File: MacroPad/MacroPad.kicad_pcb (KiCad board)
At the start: 2 copper layers, 120 x 100 mm, 27 parts, among them SW1 CherryMX, SW10 CherryMX, SW11 CherryMX, SW12 CherryMX, SW2 CherryMX, SW3 CherryMX, SW4 CherryMX, SW5 CherryMX, SW6 CherryMX, SW7 CherryMX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

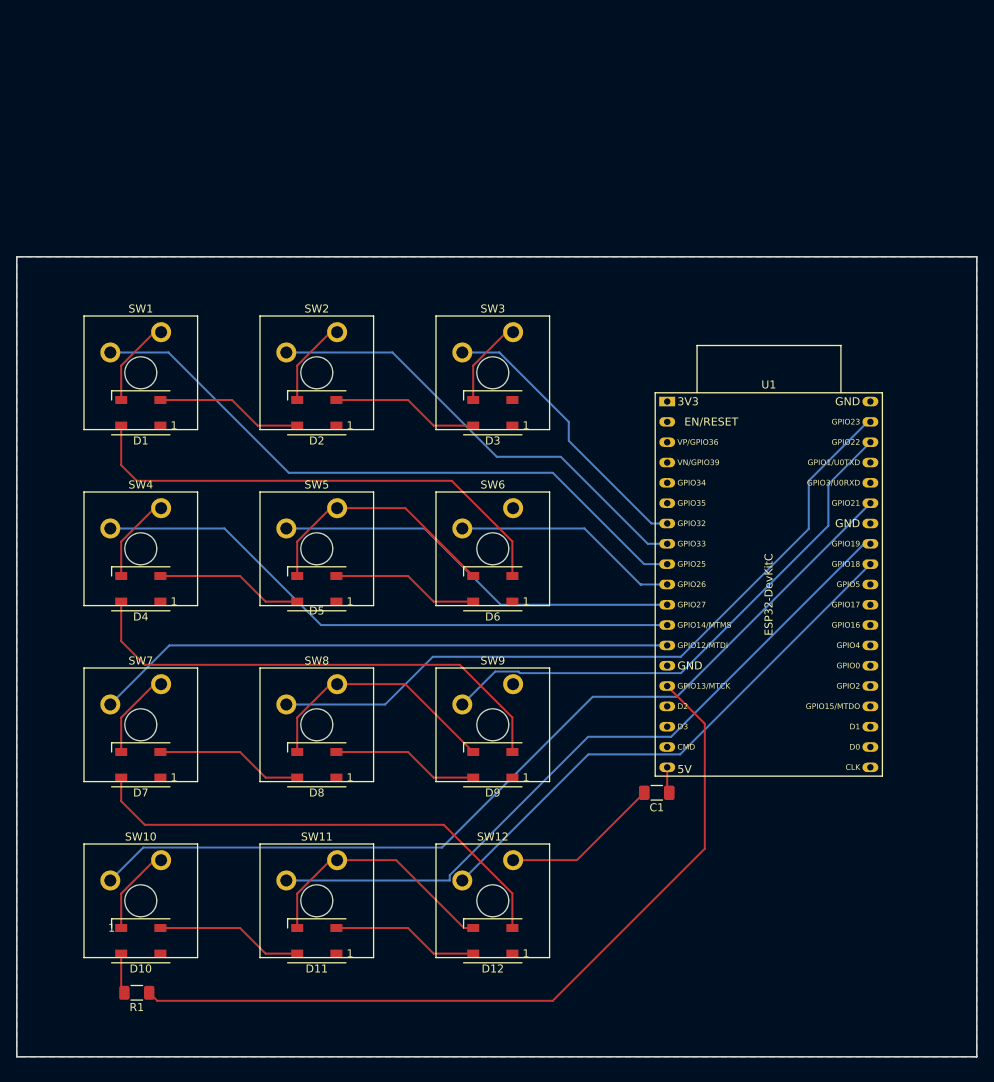
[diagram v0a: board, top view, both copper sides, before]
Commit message: updated PCB (esp at top now)
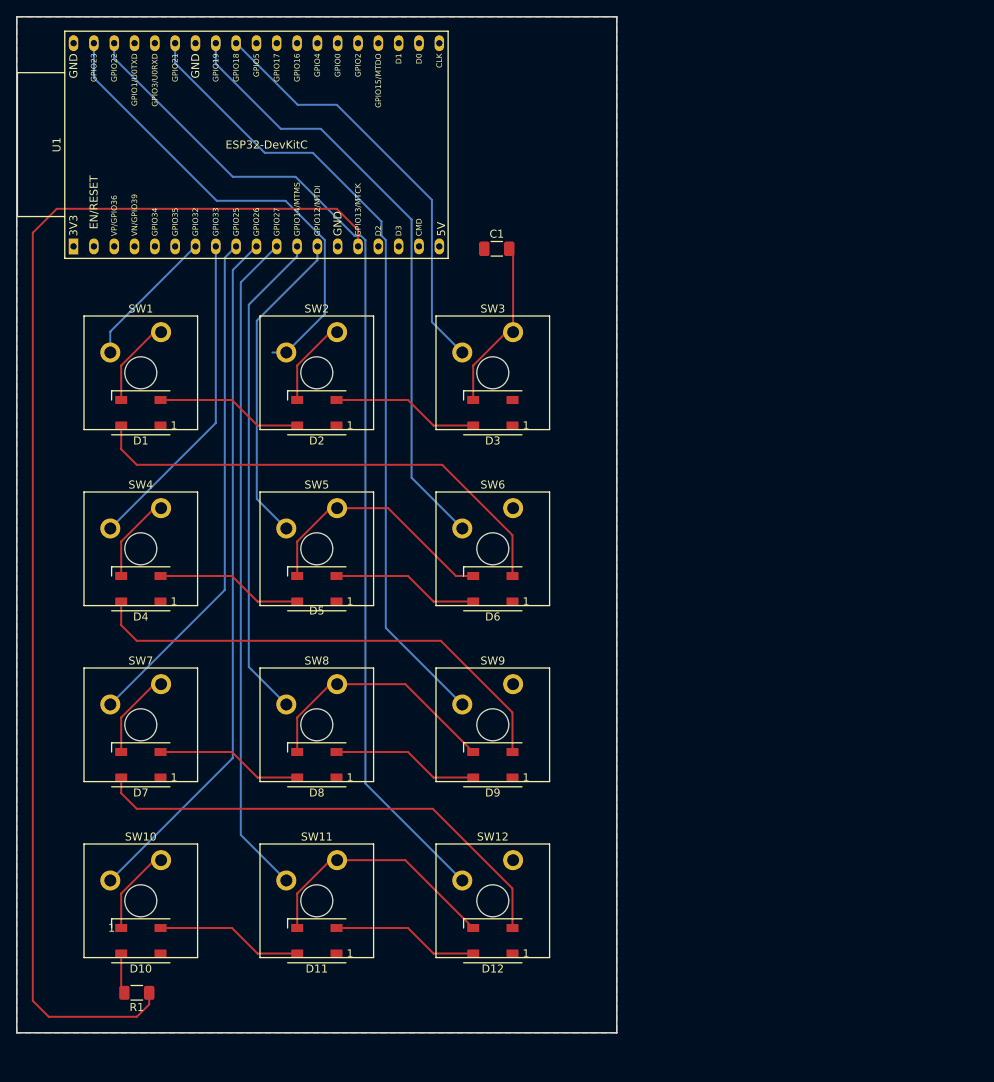
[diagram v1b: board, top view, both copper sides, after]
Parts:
- moved U1 76.7 mm to (109.1, 82.7), turned to 90 degrees
- moved C1 70.9 mm to (162.0, 83.0), turned to 0 degrees
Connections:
- U1 pad 10: SW6 -> SW10
- U1 pad 11: SW5 -> SW11
- U1 pad 12: SW4 -> SW8
- U1 pad 13: SW7 -> SW5
- U1 pad 30: SW12 -> SW3
- U1 pad 31: SW11 -> SW6
- U1 pad 33: SW10 -> SW9
- U1 pad 36: SW9 -> SW12
- U1 pad 37: SW8 -> SW2
- U1 pad 38: unconnected-(U1-Pad38) -> GND
- U1 pad 7: SW3 -> SW1
- U1 pad 8: SW2 -> SW4
- U1 pad 9: SW1 -> SW7
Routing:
- net SW1: track 80.6 -> 17.7 mm
- net SW12: track 67.4 -> 127.8 mm
- net DATA: track 100.0 -> 158.5 mm
- net SW6: track 28.5 -> 76.4 mm
- net SW4: track 74.6 -> 40.7 mm
- net SW9: track 67.8 -> 101.0 mm
- net SW8: track 91.2 -> 61.7 mm
- net SW10: track 114.5 -> 86.8 mm
- net SW3: track 35.8 -> 53.2 mm
- net SW5: track 51.6 -> 39.9 mm
- net GND: track 180.7 -> 171.4 mm
- net SW7: track 72.7 -> 63.8 mm
- net SW11: track 90.8 -> 83.5 mm
- net Net-(C1-Pad1): track 3.29 -> 0.42 mm
- net SW2: track 57.5 -> 59.4 mm
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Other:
- board size 120 x 100 mm -> 75 x 127 mm

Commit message: updated materials list
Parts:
- added O1: SSD1306, Connector_PinSocket_2.54mm:PinSocket_1x04_P2.54mm_Vertical, F.Cu at (173.0, 78.8)
- U1: moved to B.Cu
- moved U1 42.7 mm to (149.7, 95.7)
- moved C1 16.1 mm to (160.5, 99.0)
- moved D1 12.3 mm to (120.0, 115.5)
- moved SW1 12.3 mm to (120.0, 110.5)
- moved D3 12.1 mm to (160.0, 115.5)
- moved SW3 12.1 mm to (160.0, 110.5)
- moved D2 12.0 mm to (140.0, 115.5)
- moved SW2 12.0 mm to (140.0, 110.5)
- moved R1 11.0 mm to (106.0, 175.5), turned to -90 degrees
- moved D4 10.3 mm to (120.0, 135.5)
- moved SW4 10.3 mm to (120.0, 130.5)
- moved D6 10.1 mm to (160.0, 135.5)
- moved SW6 10.1 mm to (160.0, 130.5)
- moved D5 10.0 mm to (140.0, 135.5)
- moved SW5 10.0 mm to (140.0, 130.5)
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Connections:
- U1 pad 10: SW10 -> SW6
- U1 pad 11: SW11 -> SW9
- U1 pad 12: SW8 -> SW12
- U1 pad 13: SW5 -> SW2
- U1 pad 25: unconnected-(U1-Pad25) -> SW1
- U1 pad 26: unconnected-(U1-Pad26) -> SW4
- U1 pad 27: unconnected-(U1-Pad27) -> SW7
- U1 pad 28: unconnected-(U1-Pad28) -> SW10
- U1 pad 29: unconnected-(U1-Pad29) -> SW11
- U1 pad 30: SW3 -> SW8
- U1 pad 31: SW6 -> SW5
- U1 pad 33: SW9 -> Net-(U1-Pad33)
- U1 pad 36: SW12 -> Net-(U1-Pad36)
- U1 pad 37: SW2 -> unconnected-(U1-Pad37)
- U1 pad 7: SW1 -> unconnected-(U1-Pad7)
- U1 pad 8: SW4 -> unconnected-(U1-Pad8)
- U1 pad 9: SW7 -> SW3
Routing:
- net GND: track 171.4 -> 0.00 mm
- net DATA: track 158.5 -> 0.00 mm
- net SW12: track 127.8 -> 0.00 mm
- net SW9: track 101.0 -> 0.00 mm
- net SW10: track 86.8 -> 0.00 mm
- net SW11: track 83.5 -> 0.00 mm
- net SW6: track 76.4 -> 0.00 mm
- net SW7: track 63.8 -> 0.00 mm
- net SW8: track 61.7 -> 0.00 mm
- net Net-(D1-Pad4): track 61.4 -> 0.00 mm
- net Net-(D4-Pad4): track 61.3 -> 0.00 mm
- net Net-(D12-Pad2): track 60.7 -> 0.00 mm
- net SW2: track 59.4 -> 0.00 mm
- net SW3: track 53.2 -> 0.00 mm
- net SW4: track 40.7 -> 0.00 mm
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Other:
- board size 75 x 127 mm -> 75 x 118 mm

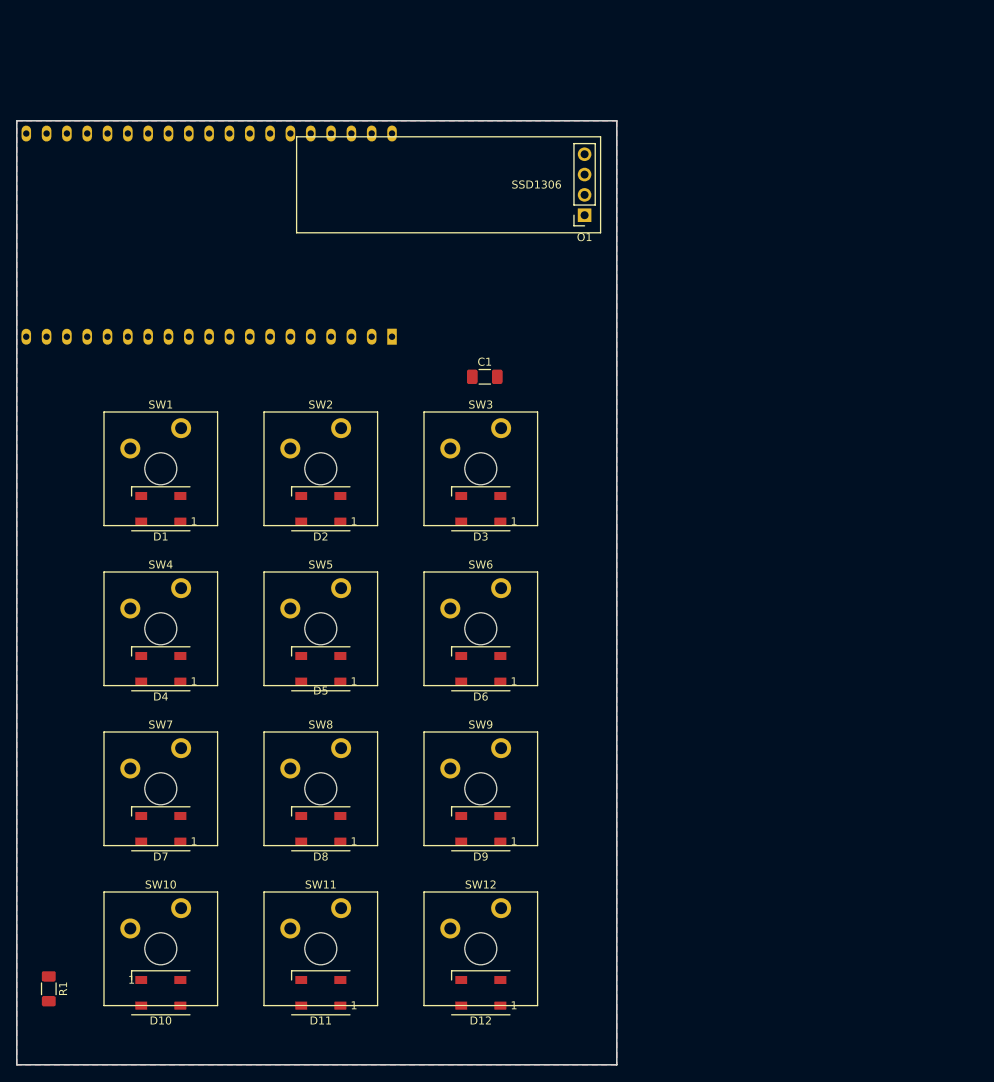
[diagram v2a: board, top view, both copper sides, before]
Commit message: redesign, added buttons and rotary encoder
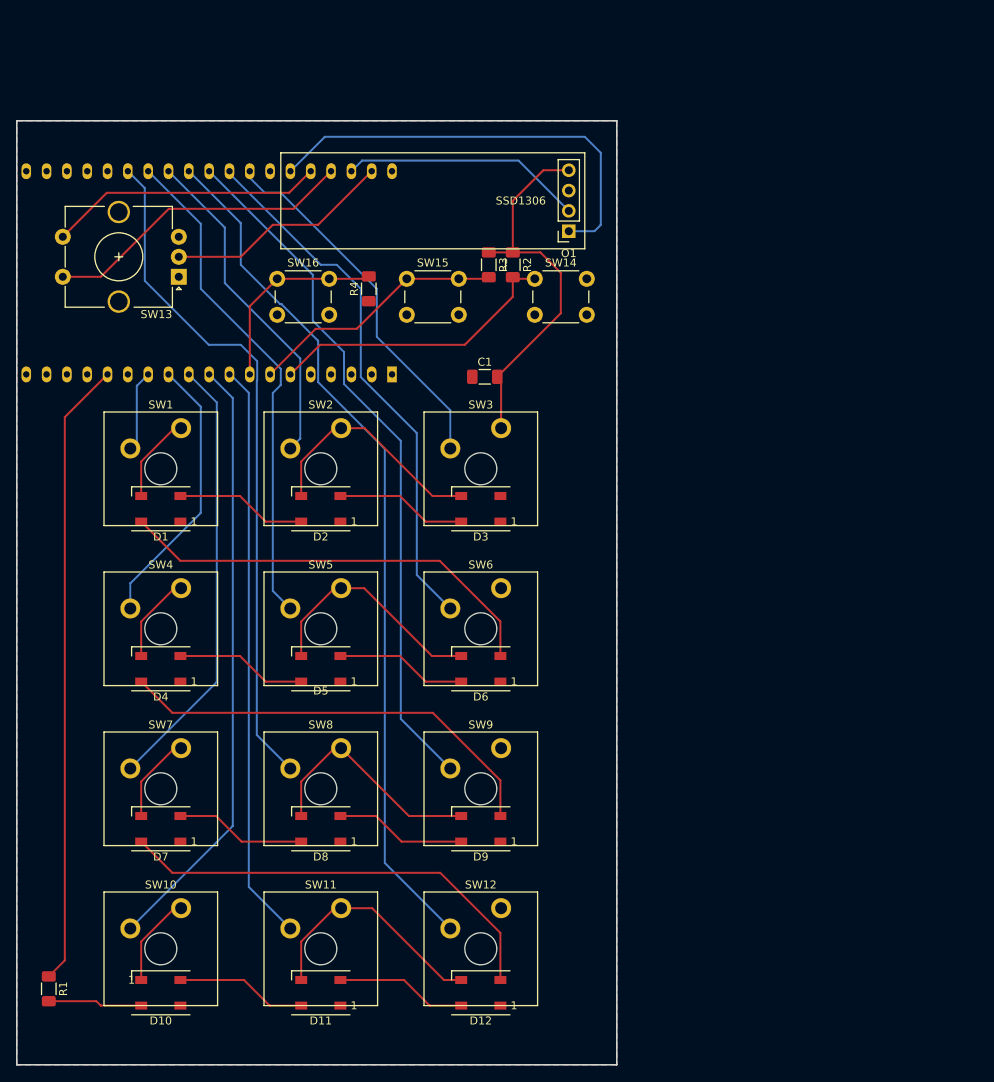
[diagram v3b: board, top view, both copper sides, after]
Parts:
- added R2: 10k, Resistor_SMD:R_1206_3216Metric_Pad1.30x1.75mm_HandSolder, F.Cu at (164.0, 85.0)
- added R3: 10k, Resistor_SMD:R_1206_3216Metric_Pad1.30x1.75mm_HandSolder, F.Cu at (161.0, 85.0)
- added R4: 10k, Resistor_SMD:R_1206_3216Metric_Pad1.30x1.75mm_HandSolder, F.Cu at (146.0, 88.0)
- added SW13: RotaryEncoder_Switch, Rotary_Encoder:RotaryEncoder_Alps_EC12E-Switch_Vertical_H20mm_CircularMountingHoles, F.Cu at (122.2, 86.5)
- added SW14: SW_Push, Button_Switch_THT:SW_PUSH_6mm, F.Cu at (166.8, 86.8)
- added SW15: SW_Push, Button_Switch_THT:SW_PUSH_6mm, F.Cu at (150.8, 86.8)
- added SW16: SW_Push, Button_Switch_THT:SW_PUSH_6mm, F.Cu at (134.6, 86.8)
- moved U1 3.10 mm to (148.9, 98.7)
- moved O1 2.81 mm to (171.0, 80.8)
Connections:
- U1 pad 10: SW6 -> SW10
- U1 pad 11: SW9 -> SW7
- U1 pad 12: SW12 -> SW4
- U1 pad 13: SW2 -> SW1
- U1 pad 25: SW1 -> SW8
- U1 pad 26: SW4 -> SW5
- U1 pad 27: SW7 -> SW2
- U1 pad 28: SW10 -> SW12
- U1 pad 29: SW11 -> SW9
- U1 pad 30: SW8 -> SW6
- U1 pad 31: SW5 -> SW3
- U1 pad 34: unconnected-(U1-Pad34) -> S2
- U1 pad 35: unconnected-(U1-Pad35) -> S1
- U1 pad 37: unconnected-(U1-Pad37) -> PinC
- U1 pad 6: unconnected-(U1-Pad6) -> Button1
- U1 pad 7: unconnected-(U1-Pad7) -> Button2
- U1 pad 8: unconnected-(U1-Pad8) -> Button3
- U1 pad 9: SW3 -> SW11
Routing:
- net GND: track 0.00 -> 212.3 mm
- net SW12: track 0.00 -> 108.3 mm
- net SW9: track 0.00 -> 87.1 mm
- net SW8: track 0.00 -> 85.5 mm
- net DATA: track 0.00 -> 78.3 mm
- net SW10: track 0.00 -> 75.8 mm
- net SW11: track 0.00 -> 72.5 mm
- net SW6: track 0.00 -> 67.3 mm
- net SW5: track 0.00 -> 62.8 mm
- net Net-(D12-Pad2): track 0.00 -> 55.5 mm
- net SW7: track 0.00 -> 55.2 mm
- net Net-(O1-Pad1): track 0.00 -> 54.7 mm
- net Net-(D4-Pad4): track 0.00 -> 54.5 mm
- net Net-(D1-Pad4): track 0.00 -> 54.4 mm
- net SW3: track 0.00 -> 46.2 mm
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
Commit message: moved R1 into an aesthetically better position
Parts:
- moved R1 4.03 mm to (110.0, 176.0)
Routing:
- net Net-(D10-Pad4): track 11.8 -> 7.57 mm
- net DATA: track 78.3 -> 77.1 mm
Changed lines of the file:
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@@
   )
   (footprint "Resistor_SMD:R_1206_3216Metric_Pad1.30x1.75mm_HandSolder" (layer "F.Cu")
-    (at 106 175.5 -90)
+    (at 110 176 -90)
     (descr "Resistor SMD 1206 (3216 Metric), square (rectangular) end terminal, IPC_7351 nominal with elongated pad for handsoldering. (Body size source: IPC-SM-782 page 72, https://www.pcb-3d.com/wordpress/wp-content/uploads/ipc-sm-782a_amendment_1_and_2.pdf), generated with kicad-footprint-generator")
     (tags "resistor handsolder")
@@
   (segment (start 146.9 153.9) (end 142.45 153.9) (width 0.25) (layer "F.Cu") (net 12))
   (segment (start 157.55 157.1) (end 150.1 157.1) (width 0.25) (layer "F.Cu") (net 12))
-  (segment (start 111.95 177.05) (end 112.5 177.6) (width 0.25) (layer "F.Cu") (net 13))
-  (segment (start 112.5 177.6) (end 117.55 177.6) (width 0.25) (layer "F.Cu") (net 13))
-  (segment (start 106 177.05) (end 111.95 177.05) (width 0.25) (layer "F.Cu") (net 13))
+  (segment (start 117.55 177.6) (end 110.05 177.6) (width 0.25) (layer "F.Cu") (net 13))
+  (segment (start 110.05 177.6) (end 110 177.55) (width 0.25) (layer "F.Cu") (net 13))
   (segment (start 122.45 174.4) (end 130.4 174.4) (width 0.25) (layer "F.Cu") (net 14))
   (segment (start 130.4 174.4) (end 133.6 177.6) (width 0.25) (layer "F.Cu") (net 14))
@@
   (segment (start 142.45 174.4) (end 150.4 174.4) (width 0.25) (layer "F.Cu") (net 15))
   (segment (start 150.4 174.4) (end 153.6 177.6) (width 0.25) (layer "F.Cu") (net 15))
-  (segment (start 108 171.95) (end 108 104.04344) (width 0.25) (layer "F.Cu") (net 16))
-  (segment (start 108 104.04344) (end 113.34344 98.7) (width 0.25) (layer "F.Cu") (net 16))
-  (segment (start 106 173.95) (end 108 171.95) (width 0.25) (layer "F.Cu") (net 16))
+  (segment (start 110 174.45) (end 110 102.04344) (width 0.25) (layer "F.Cu") (net 16))
+  (segment (start 110 102.04344) (end 113.34344 98.7) (width 0.25) (layer "F.Cu") (net 16))
   (segment (start 117 100.12344) (end 118.42344 98.7) (width 0.25) (layer "B.Cu") (net 17))
   (segment (start 116.19 107.96) (end 117 107.15) (width 0.25) (layer "B.Cu") (net 17))
